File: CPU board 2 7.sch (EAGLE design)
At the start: 58 parts, among them U1 74HC245, U10 74HC08, U11 74HC32, U12 SST39SF010, U13 AS6C62256, U14 SST39SF010, U15 SST39SF010, U2 74HC245, U3 74HC245, U4 TL7705, U6 74HC138, U7 74HC74, U8 74HC11, U9 74HC02

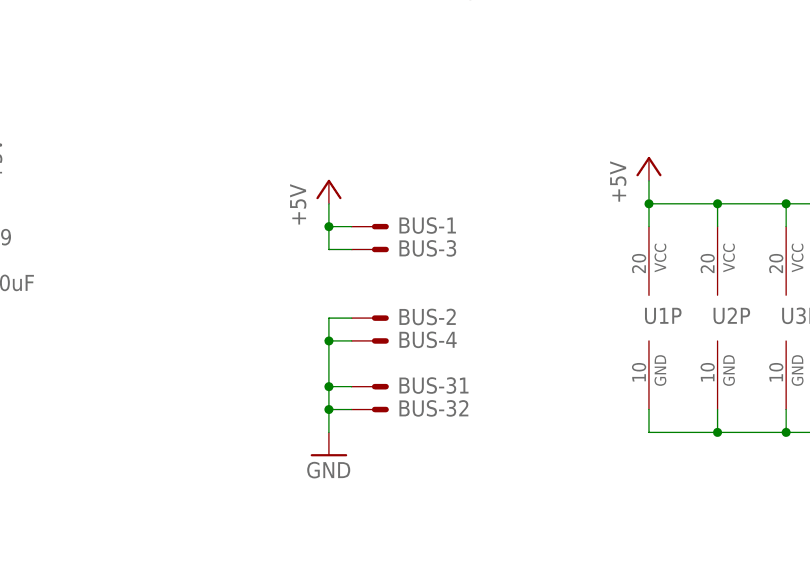
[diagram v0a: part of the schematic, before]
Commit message: Finalise bus power pin assignments
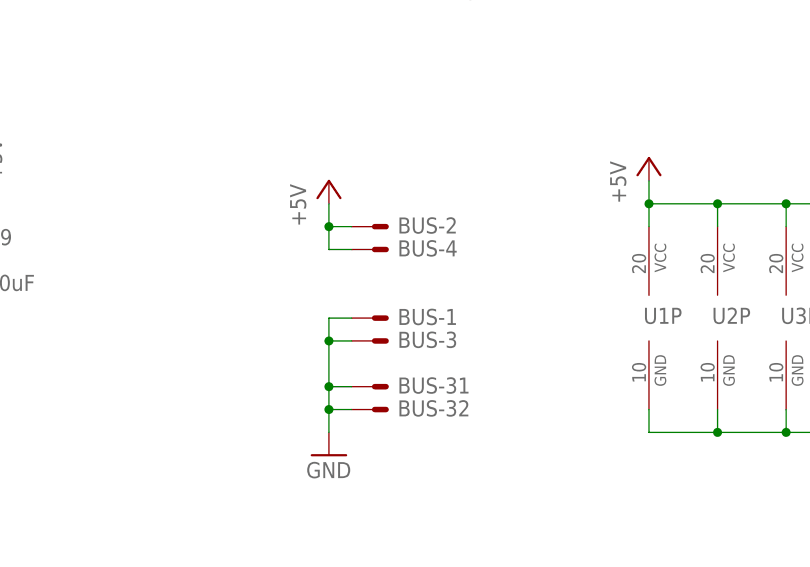
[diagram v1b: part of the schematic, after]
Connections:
- net +5V: now also BUS-2.S, BUS-4.S; no longer BUS-1.S, BUS-3.S
- net GND: now also BUS-1.S, BUS-3.S; no longer BUS-2.S, BUS-4.S
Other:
- moved on the sheet: BUS-1, BUS-2, BUS-3, BUS-4
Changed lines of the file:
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@@
 <attribute name="VALUE" x="35.56" y="-7.62" size="1.778" layer="96" rot="MR90"/>
 </instance>
-<instance part="BUS" gate="-1" x="78.74" y="-12.7" smashed="yes">
+<instance part="BUS" gate="-1" x="78.74" y="-22.86" smashed="yes">
+<attribute name="NAME" x="81.28" y="-23.622" size="1.778" layer="95"/>
+<attribute name="VALUE" x="78.486" y="-25.781" size="1.778" layer="96"/>
+</instance>
+<instance part="BUS" gate="-2" x="78.74" y="-12.7" smashed="yes">
 <attribute name="NAME" x="81.28" y="-13.462" size="1.778" layer="95"/>
 <attribute name="VALUE" x="78.486" y="-15.621" size="1.778" layer="96"/>
 </instance>
-<instance part="BUS" gate="-2" x="78.74" y="-22.86" smashed="yes">
-<attribute name="NAME" x="81.28" y="-23.622" size="1.778" layer="95"/>
-<attribute name="VALUE" x="78.486" y="-25.781" size="1.778" layer="96"/>
-</instance>
-<instance part="BUS" gate="-3" x="78.74" y="-15.24" smashed="yes">
+<instance part="BUS" gate="-3" x="78.74" y="-25.4" smashed="yes">
+<attribute name="NAME" x="81.28" y="-26.162" size="1.778" layer="95"/>
+<attribute name="VALUE" x="78.486" y="-28.321" size="1.778" layer="96"/>
+</instance>
+<instance part="BUS" gate="-4" x="78.74" y="-15.24" smashed="yes">
 <attribute name="NAME" x="81.28" y="-16.002" size="1.778" layer="95"/>
 <attribute name="VALUE" x="78.486" y="-18.161" size="1.778" layer="96"/>
-</instance>
-<instance part="BUS" gate="-4" x="78.74" y="-25.4" smashed="yes">
-<attribute name="NAME" x="81.28" y="-26.162" size="1.778" layer="95"/>
-<attribute name="VALUE" x="78.486" y="-28.321" size="1.778" layer="96"/>
 </instance>
 <instance part="BUS" gate="-5" x="469.9" y="162.56" smashed="yes">
@@
 <pinref part="GND2" gate="1" pin="GND"/>
 <wire x1="73.66" y1="-35.56" x2="73.66" y2="-33.02" width="0.1524" layer="91"/>
-<pinref part="BUS" gate="-2" pin="S"/>
 <wire x1="73.66" y1="-33.02" x2="73.66" y2="-30.48" width="0.1524" layer="91"/>
 <wire x1="73.66" y1="-30.48" x2="73.66" y2="-25.4" width="0.1524" layer="91"/>
 <wire x1="73.66" y1="-25.4" x2="73.66" y2="-22.86" width="0.1524" layer="91"/>
-<wire x1="73.66" y1="-22.86" x2="76.2" y2="-22.86" width="0.1524" layer="91"/>
-<pinref part="BUS" gate="-4" pin="S"/>
-<wire x1="76.2" y1="-25.4" x2="73.66" y2="-25.4" width="0.1524" layer="91"/>
-<junction x="73.66" y="-25.4"/>
 <pinref part="BUS" gate="-31" pin="S"/>
 <wire x1="76.2" y1="-30.48" x2="73.66" y2="-30.48" width="0.1524" layer="91"/>
@@
 <wire x1="76.2" y1="-33.02" x2="73.66" y2="-33.02" width="0.1524" layer="91"/>
 <junction x="73.66" y="-33.02"/>
+<pinref part="BUS" gate="-1" pin="S"/>
+<wire x1="73.66" y1="-22.86" x2="76.2" y2="-22.86" width="0.1524" layer="91"/>
+<pinref part="BUS" gate="-3" pin="S"/>
+<wire x1="73.66" y1="-25.4" x2="76.2" y2="-25.4" width="0.1524" layer="91"/>
+<junction x="73.66" y="-25.4"/>
 </segment>
 <segment>
@@
 <wire x1="73.66" y1="-12.7" x2="73.66" y2="-10.16" width="0.1524" layer="91"/>
 <wire x1="73.66" y1="-15.24" x2="73.66" y2="-12.7" width="0.1524" layer="91"/>
-<pinref part="BUS" gate="-1" pin="S"/>
-<wire x1="76.2" y1="-12.7" x2="73.66" y2="-12.7" width="0.1524" layer="91"/>
+<pinref part="BUS" gate="-2" pin="S"/>
+<wire x1="73.66" y1="-12.7" x2="76.2" y2="-12.7" width="0.1524" layer="91"/>
 <junction x="73.66" y="-12.7"/>
-<pinref part="BUS" gate="-3" pin="S"/>
-<wire x1="76.2" y1="-15.24" x2="73.66" y2="-15.24" width="0.1524" layer="91"/>
-</segment>
-<segment>
+<pinref part="BUS" gate="-4" pin="S"/>
+<wire x1="73.66" y1="-15.24" x2="76.2" y2="-15.24" width="0.1524" layer="91"/>
+</segment>
+<segment>

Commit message: RESET/ should not be buffered from CPU to bus
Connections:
- removed net N$34: BUS-6.S, U3A.A7
- net !RESET!: now also BUS-6.S
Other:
- moved on the sheet: BUS-6
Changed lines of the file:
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@@
 <attribute name="VALUE" x="469.646" y="159.639" size="1.778" layer="96"/>
 </instance>
-<instance part="BUS" gate="-6" x="469.9" y="165.1" smashed="yes">
-<attribute name="NAME" x="472.44" y="164.338" size="1.778" layer="95"/>
-<attribute name="VALUE" x="469.646" y="162.179" size="1.778" layer="96"/>
+<instance part="BUS" gate="-6" x="17.78" y="78.74" smashed="yes" rot="R180">
+<attribute name="NAME" x="15.24" y="79.502" size="1.778" layer="95" rot="R180"/>
+<attribute name="VALUE" x="18.034" y="81.661" size="1.778" layer="96" rot="R180"/>
 </instance>
 <instance part="BUS" gate="-7" x="469.9" y="170.18" smashed="yes">
@@
 <wire x1="109.22" y1="190.5" x2="73.66" y2="190.5" width="0.762" layer="92"/>
 <wire x1="73.66" y1="190.5" x2="71.12" y2="187.96" width="0.762" layer="92"/>
-<wire x1="71.12" y1="187.96" x2="71.12" y2="86.36" width="0.762" layer="92"/>
+<wire x1="71.12" y1="187.96" x2="71.12" y2="81.28" width="0.762" layer="92"/>
 <wire x1="111.76" y1="187.96" x2="114.3" y2="190.5" width="0.762" layer="92"/>
 <wire x1="114.3" y1="190.5" x2="187.96" y2="190.5" width="0.762" layer="92"/>
@@
 <pinref part="U3" gate="A" pin="B7"/>
 </segment>
+<segment>
+<wire x1="71.12" y1="81.28" x2="68.58" y2="78.74" width="0.1524" layer="91"/>
+<pinref part="BUS" gate="-6" pin="S"/>
+<wire x1="68.58" y1="78.74" x2="20.32" y2="78.74" width="0.1524" layer="91"/>
+<label x="22.86" y="78.74" size="1.778" layer="95"/>
+</segment>
 </net>
 <net name="!BUSRQ!" class="0">
@@
 </segment>
 </net>
-<net name="N$34" class="0">
-<segment>
-<pinref part="U3" gate="A" pin="A7"/>
-<pinref part="BUS" gate="-6" pin="S"/>
-<wire x1="467.36" y1="165.1" x2="462.28" y2="165.1" width="0.1524" layer="91"/>
-</segment>
-</net>

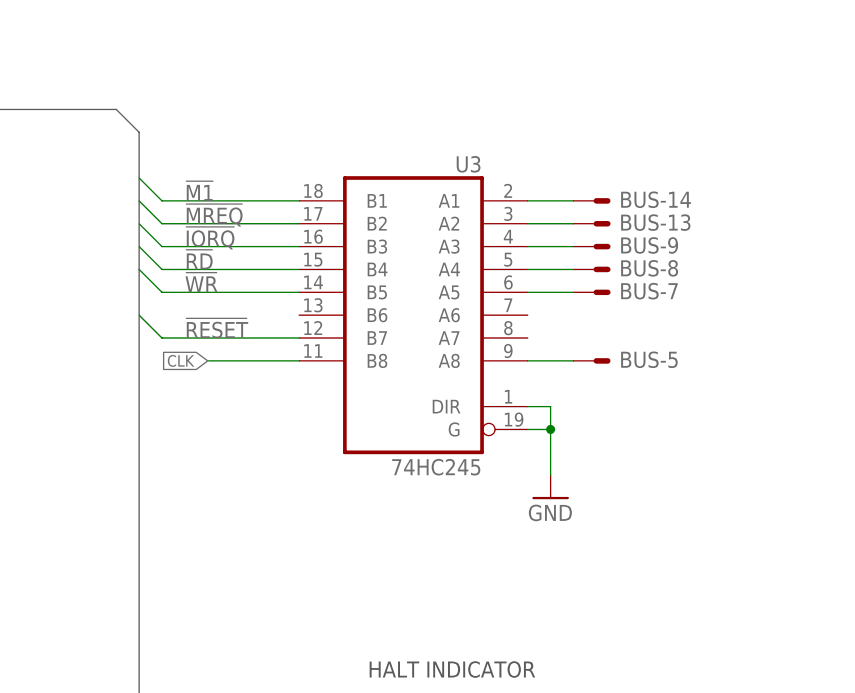
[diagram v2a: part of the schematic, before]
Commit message: Ground unused pin 13 on U3
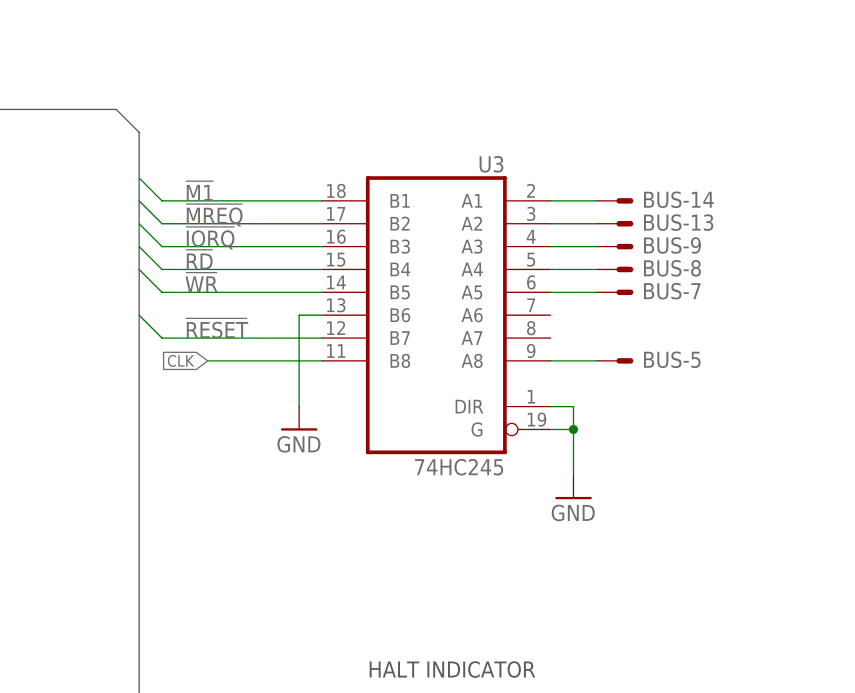
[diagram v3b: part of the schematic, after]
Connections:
- net GND: now also U3A.B6
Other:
- moved on the sheet: BUS-13, BUS-14, BUS-5, BUS-7, BUS-8, BUS-9, U3

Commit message: Fix DATA bus direction logic
Off-board peripherals, e.g. CTC, need to see a certain sequence of byte reads (RETI instruction) in order to release interrupt. Original direction logic for the DATA bus did not permit this to happen.
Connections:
- removed net !OBD!: U1A.G, U9C.O
- removed net N$40: U11A.I0, U9A.O
- removed net N$43: U11A.I1, U9B.O
- net !IORQ!: no longer U10A.I1, U9A.I0
- net !M1!: no longer U9A.I1
- net !MREQ!: no longer U10A.I0
- net !RD!: now also U11A.I0; no longer U9B.I1, U9C.I0
- net !WR!: now also U10A.I0
- net DIR: now also U10A.O; no longer U11A.O
- net GND: now also U1A.G, U9A.I0, U9A.I1, U9B.I0, U9B.I1, U9C.I0, U9C.I1
- net N$20: now also U10B.O, U11A.I1; no longer U10A.O, U9B.I0
- net N$21: now also U10A.I1, U11A.O; no longer U10B.O, U9C.I1
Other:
- note removed: "DIRECTION SHOULD BE IN TO THE PROCESSOR (HIGH) FOR OFF-BOARD READS AND INTERRUPT ACKNOWLEDGEMENTS."
- moved on the sheet: JP2, RN1-1, RN1-2, RN1-3, RN1-4, RN1-5, RN1-6, RN1-7, RN1-8, RN1_, U10A, U10B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

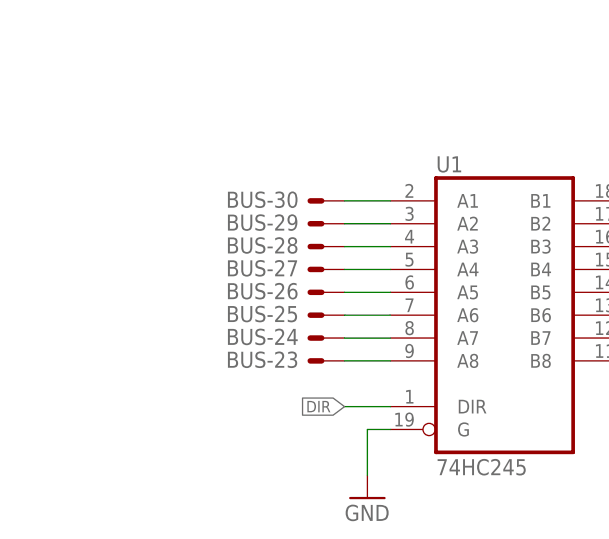
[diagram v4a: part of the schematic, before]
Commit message: Add pull-downs to bus side of DATA buffer
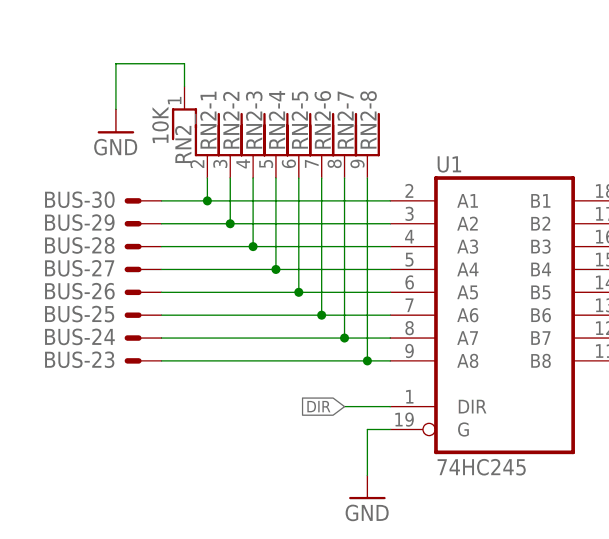
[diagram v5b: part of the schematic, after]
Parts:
- added RN2: 10K, resistor-net:RNX8
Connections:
- net GND: now also RN2_.1
- net N$25: now also RN2-8.1
- net N$26: now also RN2-7.1
- net N$27: now also RN2-6.1
- net N$28: now also RN2-5.1
- net N$29: now also RN2-4.1
- net N$30: now also RN2-3.1
- net N$31: now also RN2-2.1
- net N$32: now also RN2-1.1
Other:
- moved on the sheet: BUS-23, BUS-24, BUS-25, BUS-26, BUS-27, BUS-28, BUS-29, BUS-30

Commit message: Slight re-arrangement
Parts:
- U5: value (none) -> Z80
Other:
- moved on the sheet: JP2, QG1, R10, R11, R12, R13, R14, R2, R5, R6, R7, R8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

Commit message: RESET/ not buffered via U3 any more
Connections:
- net !RESET!: no longer U3A.B7
- net GND: now also U3A.B7
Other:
- note removed: "* CHECK CLEANLINESS OF CLOCK SIGNAL AFTER LOADING"
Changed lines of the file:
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@@
 <text x="431.8" y="50.8" size="1.778" layer="97" align="bottom-center">SLOW ROM</text>
 <text x="119.38" y="71.12" size="1.778" layer="97" align="bottom-center">POWER ON RESET</text>
-<text x="60.96" y="-109.22" size="2.54" layer="97">* CHECK CLEANLINESS OF CLOCK SIGNAL AFTER LOADING</text>
 <text x="444.5" y="119.38" size="1.778" layer="97">HALT INDICATOR
 GREEN  CPU RUNNING
@@
 <pinref part="U3" gate="A" pin="B6"/>
 <wire x1="439.42" y1="167.64" x2="436.88" y2="167.64" width="0.1524" layer="91"/>
-<wire x1="436.88" y1="167.64" x2="436.88" y2="157.48" width="0.1524" layer="91"/>
+<wire x1="436.88" y1="167.64" x2="436.88" y2="165.1" width="0.1524" layer="91"/>
 <pinref part="GND16" gate="1" pin="GND"/>
+<pinref part="U3" gate="A" pin="B7"/>
+<wire x1="436.88" y1="165.1" x2="436.88" y2="157.48" width="0.1524" layer="91"/>
+<wire x1="439.42" y1="165.1" x2="436.88" y2="165.1" width="0.1524" layer="91"/>
+<junction x="436.88" y="165.1"/>
 </segment>
 <segment>
@@
 </segment>
 <segment>
-<wire x1="439.42" y1="165.1" x2="421.64" y2="165.1" width="0.1524" layer="91"/>
-<wire x1="421.64" y1="165.1" x2="419.1" y2="167.64" width="0.1524" layer="91"/>
-<label x="424.18" y="165.1" size="1.778" layer="95"/>
-<pinref part="U3" gate="A" pin="B7"/>
-</segment>
-<segment>

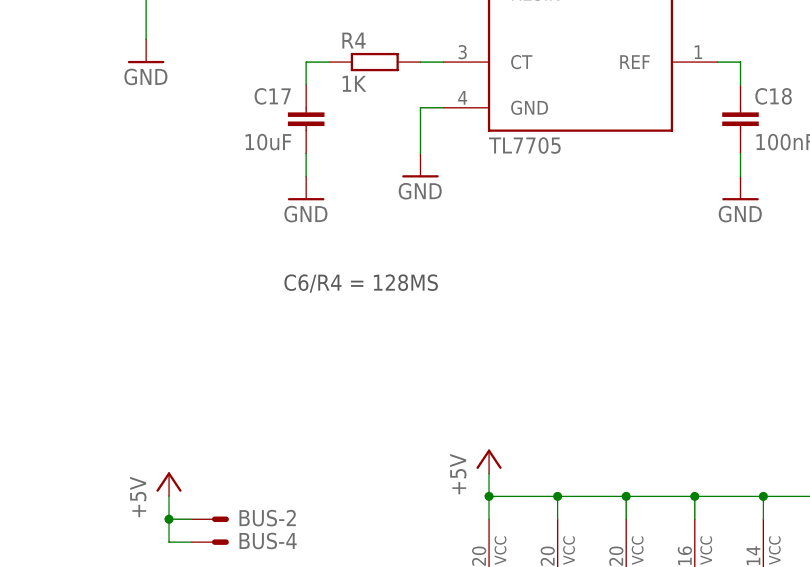
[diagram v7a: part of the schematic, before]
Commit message: Update component desigator in RC calc for POR
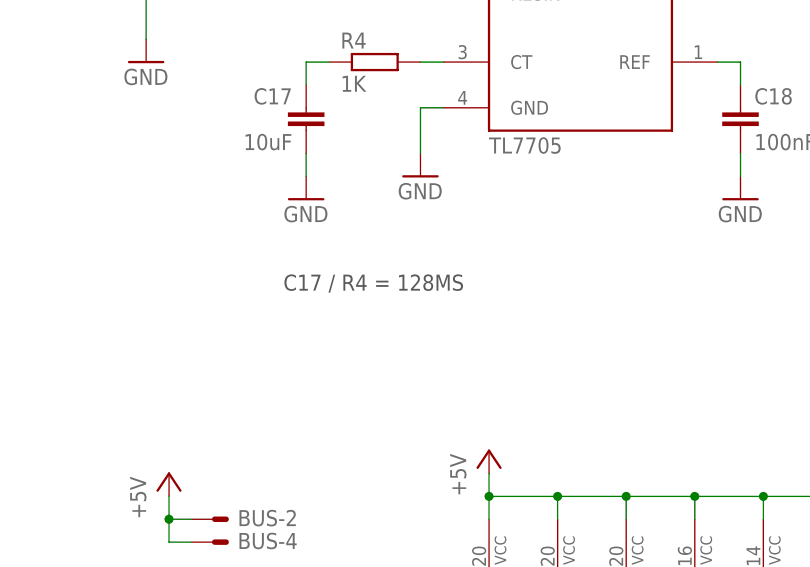
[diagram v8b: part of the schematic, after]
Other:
- note added: "C17 / R4 = 128MS"
- note removed: "C6/R4 = 128MS"
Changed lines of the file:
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@@
 <sheet>
 <plain>
-<text x="86.36" y="12.7" size="1.778" layer="97">C6/R4 = 128MS</text>
+<text x="86.36" y="12.7" size="1.778" layer="97">C17 / R4 = 128MS</text>
 <text x="317.5" y="182.88" size="1.778" layer="97" align="bottom-center">APP ROM</text>
 <text x="342.9" y="182.88" size="1.778" layer="97" align="bottom-center">RAM</text>
